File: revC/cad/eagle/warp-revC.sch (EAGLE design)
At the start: 13 parts, among them J2 QIIC connector, J3 QIIC connector, J4 DF40FC-20DP-0.4V(51), J5 CORTEX_DEBUG_SMD, U1 MAX40200, U2 MAX40200

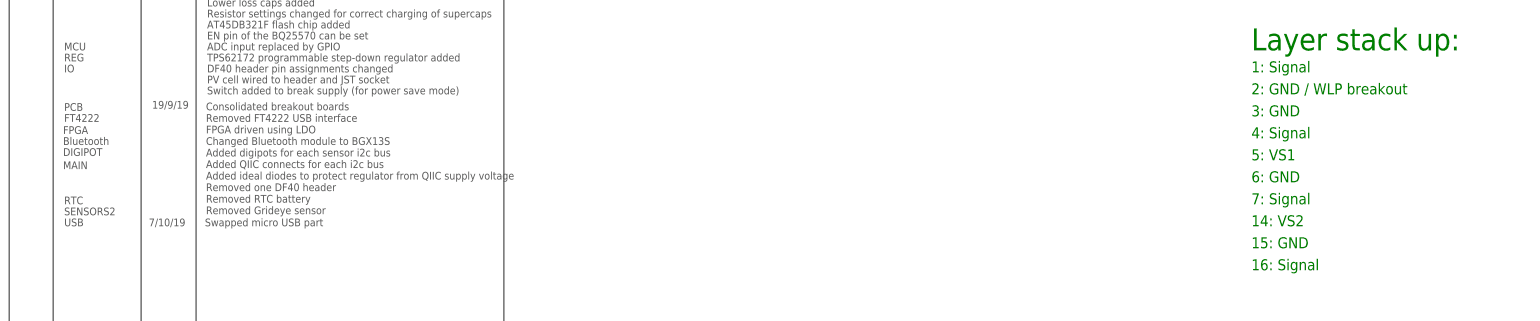
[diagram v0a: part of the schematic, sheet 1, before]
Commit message: Removed FPGA microvias and rerouted
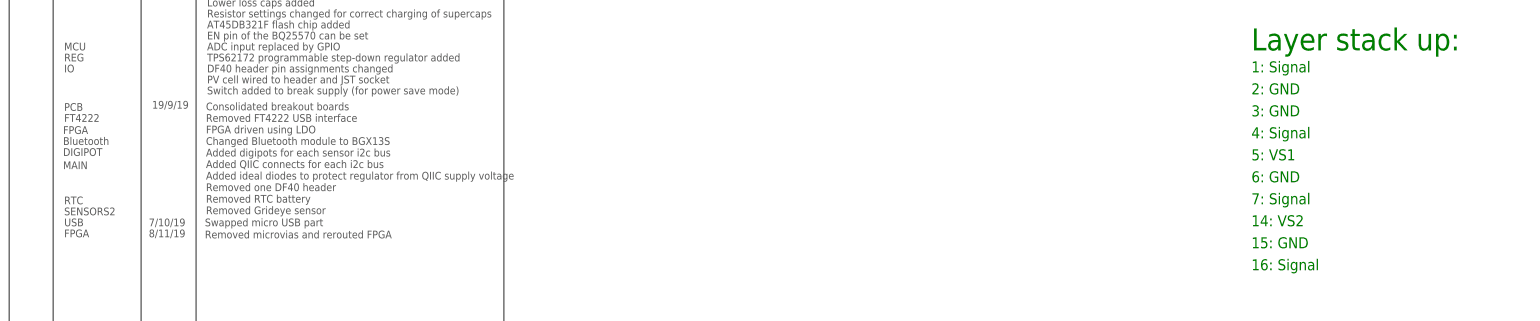
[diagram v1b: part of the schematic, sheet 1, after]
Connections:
- net GND: now also U2.IOB_25B_G3, U2.RGB1
- net VCC: now also U2.IOB_12A_G4_CDONE, U2.IOB_2A; no longer U2.VCCIO_0
- net VCC_1V2: now also U2.IOB_10A, U2.IOT_46B_G0, U2.VCCIO_0
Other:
- note added: "2: GND"
- note added: "8/11/19"
- note added: "Removed microvias and rerouted FPGA"
- note removed: "2: GND / WLP breakout"
- note removed: "USB2"
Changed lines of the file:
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@@
 <part name="C7" library="SparkFun-Passives" deviceset="CAP" device="0402-CAP" value="0.1uF"/>
 <part name="C6" library="SparkFun-Passives" deviceset="CAP" device="0402-CAP" value="10uF"/>
+<part name="GND4" library="supply1" library_urn="urn:adsk.eagle:library:371" deviceset="GND" device=""/>
+<part name="SUPPLY1" library="SparkFun-PowerSymbols" deviceset="VCC" device=""/>
+<part name="SUPPLY2" library="SparkFun-PowerSymbols" deviceset="VCC" device=""/>
+<part name="GND5" library="supply1" library_urn="urn:adsk.eagle:library:371" deviceset="GND" device=""/>
 </parts>
 <sheets>
@@
 <attribute name="NAME" x="313.944" y="114.681" size="1.778" layer="95"/>
 <attribute name="VALUE" x="313.944" y="109.601" size="1.778" layer="96"/>
+</instance>
+<instance part="GND4" gate="1" x="195.58" y="116.84" smashed="yes">
+<attribute name="VALUE" x="193.04" y="114.3" size="1.778" layer="96"/>
+</instance>
+<instance part="SUPPLY1" gate="G$1" x="198.12" y="144.78" smashed="yes">
+<attribute name="VALUE" x="198.12" y="147.574" size="1.778" layer="96" align="bottom-center"/>
+</instance>
+<instance part="SUPPLY2" gate="G$1" x="182.88" y="66.04" smashed="yes">
+<attribute name="VALUE" x="182.88" y="68.834" size="1.778" layer="96" align="bottom-center"/>
+</instance>
+<instance part="GND5" gate="1" x="193.04" y="66.04" smashed="yes">
+<attribute name="VALUE" x="190.5" y="63.5" size="1.778" layer="96"/>
 </instance>
 </instances>
@@
 <pinref part="C3" gate="G$1" pin="1"/>
 </segment>
+<segment>
+<pinref part="U2" gate="G$1" pin="IOB_10A"/>
+<wire x1="175.26" y1="144.78" x2="190.5" y2="144.78" width="0.1524" layer="91"/>
+<label x="177.8" y="144.78" size="1.778" layer="95"/>
+</segment>
+<segment>
+<pinref part="U2" gate="G$1" pin="IOT_46B_G0"/>
+<wire x1="175.26" y1="76.2" x2="187.96" y2="76.2" width="0.1524" layer="91"/>
+<label x="177.8" y="76.2" size="1.778" layer="95"/>
+</segment>
+<segment>
+<pinref part="U2" gate="G$1" pin="VCCIO_0"/>
+<wire x1="175.26" y1="165.1" x2="190.5" y2="165.1" width="0.1524" layer="91"/>
+<label x="177.8" y="165.1" size="1.778" layer="95"/>
+</segment>
 </net>
 <net name="I2C1_SCL" class="0">
@@
 <pinref part="C4" gate="G$1" pin="1"/>
 <pinref part="C5" gate="G$1" pin="1"/>
+<label x="177.8" y="134.62" size="1.778" layer="95"/>
 </segment>
 </net>
@@
 <pinref part="C2" gate="G$1" pin="2"/>
 </segment>
+<segment>
+<pinref part="U2" gate="G$1" pin="IOB_25B_G3"/>
+<wire x1="175.26" y1="114.3" x2="187.96" y2="114.3" width="0.1524" layer="91"/>
+<wire x1="187.96" y1="114.3" x2="187.96" y2="121.92" width="0.1524" layer="91"/>
+<wire x1="187.96" y1="121.92" x2="195.58" y2="121.92" width="0.1524" layer="91"/>
+<wire x1="195.58" y1="121.92" x2="195.58" y2="119.38" width="0.1524" layer="91"/>
+<pinref part="GND4" gate="1" pin="GND"/>
+<label x="177.8" y="114.3" size="1.778" layer="95"/>
+</segment>
+<segment>
+<pinref part="U2" gate="G$1" pin="RGB1"/>
+<wire x1="175.26" y1="71.12" x2="180.34" y2="71.12" width="0.1524" layer="91"/>
+<wire x1="180.34" y1="71.12" x2="180.34" y2="73.66" width="0.1524" layer="91"/>
+<wire x1="180.34" y1="73.66" x2="193.04" y2="73.66" width="0.1524" layer="91"/>
+<wire x1="193.04" y1="73.66" x2="193.04" y2="68.58" width="0.1524" layer="91"/>
+<pinref part="GND5" gate="1" pin="GND"/>
+</segment>
 </net>
 <net name="CRESET_B" class="0">
@@
 <net name="VCC" class="0">
 <segment>
-<label x="177.8" y="165.1" size="1.778" layer="95"/>
-<pinref part="U2" gate="G$1" pin="VCCIO_0"/>
-<wire x1="175.26" y1="165.1" x2="198.12" y2="165.1" width="0.1524" layer="91"/>
-<wire x1="198.12" y1="165.1" x2="198.12" y2="167.64" width="0.1524" layer="91"/>
 <label x="177.8" y="160.02" size="1.778" layer="95"/>
 <pinref part="U2" gate="G$1" pin="VCCIO_2"/>
 <wire x1="198.12" y1="167.64" x2="198.12" y2="175.26" width="0.1524" layer="91"/>
 <wire x1="175.26" y1="160.02" x2="198.12" y2="160.02" width="0.1524" layer="91"/>
-<wire x1="198.12" y1="160.02" x2="198.12" y2="165.1" width="0.1524" layer="91"/>
-<junction x="198.12" y="165.1"/>
+<wire x1="198.12" y1="160.02" x2="198.12" y2="167.64" width="0.1524" layer="91"/>
 <pinref part="VCC" gate="VCC" pin="VCC"/>
 <wire x1="175.26" y1="167.64" x2="198.12" y2="167.64" width="0.1524" layer="91"/>
@@
 <wire x1="53.34" y1="157.48" x2="53.34" y2="149.86" width="0.1524" layer="91"/>
 <pinref part="P+2" gate="VCC" pin="VCC"/>
+</segment>
+<segment>
+<pinref part="U2" gate="G$1" pin="IOB_12A_G4_CDONE"/>
+<wire x1="175.26" y1="139.7" x2="198.12" y2="139.7" width="0.1524" layer="91"/>
+<wire x1="198.12" y1="139.7" x2="198.12" y2="144.78" width="0.1524" layer="91"/>
+<pinref part="SUPPLY1" gate="G$1" pin="VCC"/>
+<label x="177.8" y="139.7" size="1.778" layer="95"/>
+</segment>
+<segment>
+<pinref part="U2" gate="G$1" pin="IOB_2A"/>
+<wire x1="175.26" y1="60.96" x2="182.88" y2="60.96" width="0.1524" layer="91"/>
+<wire x1="182.88" y1="60.96" x2="182.88" y2="66.04" width="0.1524" layer="91"/>
+<pinref part="SUPPLY2" gate="G$1" pin="VCC"/>
 </segment>
 </net>
@@
 Richard Hopper</text>
 <text x="293.624" y="6.096" size="1.778" layer="94">NO WARRANTY. See LICENCE.txt</text>
-<text x="344.17" y="20.32" size="2.54" layer="94" ratio="15">USB2</text>
+<text x="344.17" y="20.32" size="2.54" layer="94" ratio="15">USB</text>
 </plain>
 <instances>
@@
 <text x="304.8" y="101.6" size="5.08" layer="91">Layer stack up:</text>
 <text x="304.8" y="96.52" size="2.54" layer="91">1: Signal</text>
-<text x="304.8" y="91.44" size="2.54" layer="91">2: GND / WLP breakout</text>
+<text x="304.8" y="91.44" size="2.54" layer="91">2: GND</text>
 <text x="304.8" y="86.36" size="2.54" layer="91">3: GND</text>
 <text x="304.8" y="60.96" size="2.54" layer="91">14: VS2</text>
@@
 <text x="50.038" y="60.96" size="1.778" layer="97">7/10/19</text>
 <text x="62.992" y="60.96" size="1.778" layer="97">Swapped micro USB part </text>
+<text x="30.48" y="58.42" size="1.778" layer="97">FPGA</text>
+<text x="50.038" y="58.42" size="1.778" layer="97">8/11/19</text>
+<text x="62.992" y="58.166" size="1.778" layer="97">Removed microvias and rerouted FPGA</text>
 </plain>
 <instances>

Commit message: MAG3110 with FXOS8700CQ. Added BOM
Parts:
- removed U1, U2: MAX40200, MAX40200:MAX40200
- added S3: EVPAYG0BAEVPAYG0BA, EVPAYG0BA:EVPAYG0BAEVPAYG0BA
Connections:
- removed net !INT: U1.!INT!
- removed net !RESET: U1.!RESET
- removed net ADXL362_SPI_CS: U1.!CS
- removed net AT45DB321F_SPI_CS: U1.PTA9, U2.!CS!
- removed net BQ24230_OUT: U1.EN2, U1.OUT, U2.IN
- removed net CAP: U2.CAP
- removed net CRESET_B: U2.CRESET_B
- removed net CTRL: U1.CTRL
- removed net DCP_RW1: U1.RW
- removed net DCP_RW3: U2.RW
- removed net EXTAL0: U1.PTA3/EXTAL0
- removed net I2C_SCL: U1.SCL, U2.I2C_SCL/SPI_SPC, U2.SCX
- removed net I2C_SCL/LPUART0_TX: U1.PTB3/IRQ_10
- removed net I2C_SDA: U1.SDA, U2.I2C_SDA/SPI_SDI/SPI3_SDO, U2.SDX
- removed net I2C_SDA/LPUART0_RX: U1.PTB4/IRQ_11
- removed net ICE40_VCC_PLL: U2.IOB_24A, U2.VCCPLL
- removed net IN: U1.IN
- removed net LBOOST: U1.LBOOST
- removed net LBUCK: U1.LBUCK
- removed net LOAD: U1.LOAD
- removed net N$1: U1.BYP, U1.ISET, U1.LFXTAL_N
- removed net N$2: U1.ILIM, U1.LFXTAL_P
- removed net N$3: U1.!PGOOD!, U1.ANTENNA, U1.EVI, U1.RF
- removed net N$4: U1.TS, U2.!WP!
- removed net N$5: U1.!CHG!
- removed net N$8: U1.TMR
- removed net OK_HYST: U1.OK_HYST
- removed net OK_PROG: U1.OK_PROG
- removed net OUT: U2.OUT
- removed net PTA0/SWD_CLK: U1.PTA0/IRQ_0/LLWU_P7
- removed net PTA1/RESET_B: S1.A, S1.A', U1.PTA1/IRQ1/LPTMR0_ALT1
- removed net PTA12: U1.PTA12/IRQ_13/LPTMR0_ALT2
- removed net PTA2/SWD_DIO: U1.PTA2
- removed net PTA5: U1.PTA5/RTC_CLK_IN
- removed net PTA8: U1.PTA8
- removed net PTB1: U1.PTB1/IRQ_6/ADC0_SE8/CMP0_IN3
- removed net PTB10: U1.PTB10
- removed net PTB11: U1.PTB11
- removed net PTB13/CLKOUT32K: U1.PTB13/CLKOUT32K
- removed net PTB2: U1.PTB2/IRQ_7
- removed net PTB5: U1.PTB5/IRQ_12
- removed net PTB6: U1.PTB6/IRQ_2/LPTMR0_ALT3
- removed net PTB7: U1.PTB7/IRQ_3
- removed net REG_LOAD: U1.IN
- removed net SPI_CS: U1.CS, U2.CS, U2.IOB_35B_SPI_SS
- removed net SPI_MISO: U1.MISO, U1.PTA6, U1.SDO, U2.IOB_32A_SPI_SO, U2.SDO, U2.SO
- removed net SPI_MOSI: U1.MOSI, U1.PTA7/IRQ_4, U1.SDI, U2.IOB_33B_SPI_SI, U2.SDI, U2.SI
- removed net SW: U1.SW
- removed net UART_CTS: U1.UART_CTS
- removed net UART_RTS: U1.UART_RTS
- removed net UART_RX: U1.UART_RX
- removed net UART_TX: U1.UART_TX
- removed net VBAT: U1.VBAT
- removed net VBAT_OV: U1.VBAT_OV
- removed net VBUS: U1.VBUS
- removed net VCC: U1.IOVDD, U1.RL, U1.VBATT, U1.VCC, U1.VDD, U1.VDDIO, U1.VLOGIC, U1.VS, U2.!RST!, U2.I2C_VS_SPI_MODE_SELECT, U2.IOB_12A_G4_CDONE, U2.IOB_2A, U2.PS, U2.RL, U2.SPI_VCCIO1, U2.VCC, U2.VCCIO_2, U2.VDD, U2.VDDIO, U2.VDD_IO, U2.VLOGIC, U2.VPP_2V5
- removed net VCC_1V2: U1.OUT, U2.IOB_10A, U2.IOT_46B_G0, U2.VCC, U2.VCCIO_0
- removed net VIN: U1.EN, U1.VIN, U1.VIN_DC
- removed net VOUT: U1.VOUT
- removed net VOUT_SET: U1.VOUT_SET
- removed net VRDIV: U1.VRDIV
- removed net VREF_SAMP: U1.VREF_SAMP
- removed net VREG: U1.IN
- removed net VSEL1: U1.VSEL1
- removed net VSEL2: U1.VSEL2
- removed net VSEL3: U1.VSEL3
- removed net VSEL4: U1.VSEL4
- removed net VSTOR: U1.VOC_SAMP, U1.VOUT_EN, U1.VSTOR
- removed net XTAL0: U1.PTA4/XTAL0
- net BAT: no longer U1.BAT
- net GND: now also S3.B, S3.B'; no longer S1.B, S1.B', U1.!CE!, U1.!EN, U1.ANT_GND, U1.CLKOE, U1.EN1, U1.GND, U1.GND@10, U1.GND@12, U1.GND@13, U1.GND@16, U1.GND@5, U1.NC17, U1.NC9, U1.PAD, U1.SA0, U1.SHIELD, U1.TD, U1.VGND, U1.VSS, U1.VSS1, U1.VSS15, U2.CSB3, U2.GND, U2.GND@12, U2.GND@13, U2.GNDA, U2.GNDIO, U2.I2C_SA0/SPI_SDO, U2.IOB_25B_G3, U2.RESERVED@10, U2.RESERVED@11, U2.RESERVED@15, U2.RESERVED@9, U2.RGB1, U2.SDO1, U2.SDO2, U2.VGND
- net I2C1_SCL: no longer U2.IOT_47A
- net I2C1_SDA: no longer U2.IOB_11B_G5
- net I2C2_SCL: no longer U2.IOT_37A
- net I2C2_SDA: no longer U2.IOT_36B
- net RTC_!INT!/RESET_B: now also S3.A, S3.A'
- net SPI_SCK: no longer U1.PTB0/IRQ_5/LLWU_P4, U1.SCK, U1.SCLK, U2.IOB_34A_SPI_SCK, U2.SCK
- net VCC_QIIC: no longer U2.IN
- net VS2: no longer U1.OUT, U2.OUT
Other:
- note added: "13/11/19"
- note added: "14/11/19"
- note added: "BLUETHOOTH"
- note added: "BOARD"
- note added: "Brought reset switch out to main sheet"
- note added: "External sensor sockets"
- note added: "Header breakout socket"
- note added: "I2C Address: 0x1E"
- note added: "Ideal dioides placed in module"
- note added: "MCU reset switch"
- note added: "MODULE ABBEVIATIONS BT: BLUETHOOTH CH: CHARGER DP: DIGIPOT FP: FPGA MP: MPU PV: BOOSTER RG: REG RT: RTC SA: SENSORS-A SB: SENSORS-B USB: USB"
- note added: "Replaced MAG3110 (obsolete) with FXOS8700CQ"
- note added: "SENSOR"
- note added: "SENSORS"
- note added: "Supply switching for FPGA"
- note removed: "Bluetooth"
- note removed: "External sensor socket"
- note removed: "Header sockets"
- note removed: "I2C Address: 0x0E"
- note removed: "PCB"
- note removed: "Reset switch"
- note removed: "SENSORS2"
- note removed: "Supply select for FPGA"
- moved on the sheet: J5

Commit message: Corrected footprint errors
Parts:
- J5: value CORTEX_DEBUG_SMD -> CORTEX_DEBUGCORTEX_DEBUG; device SparkFun-Connectors:CORTEX_DEBUG_SMD -> CORTEX_DEBUG:CORTEX_DEBUGCORTEX_DEBUG
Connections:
- net BGX13S_!RST renamed FPGA_CS
- net SI4705_!RST renamed CRESET_B
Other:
- moved on the sheet: J5

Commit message: Corrections to footprints
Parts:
- removed FD1, FD2, FD3, FD4: FIDUCIAL1X2, SparkFun-Aesthetics:FIDUCIAL1X2
- J5: value CORTEX_DEBUGCORTEX_DEBUG -> FTSH-105-01-XXX-DV-K; device CORTEX_DEBUG:CORTEX_DEBUGCORTEX_DEBUG -> FTSH-105-01-XXX-DV-K:FTSH-105-01-XXX-DV-K
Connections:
- net GND: now also J5.3, J5.5; no longer J5.GND@3, J5.GND@5
- net RTC_!INT!/RESET_B: now also J5.10; no longer J5.!RESET
- net SWD_CLK: now also J5.4; no longer J5.SWDCLK/TCK
- net SWD_DIO: now also J5.2; no longer J5.SWDIO/TMS
- net VS1: now also J5.1; no longer J5.VCC
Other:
- note removed: "Fiducial Markers"
- moved on the sheet: J5

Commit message: Commit of CAD design, BOM and datasheets for 1st production run of Warp-revC
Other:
- note added: "15/01/19"
- note added: "Corrected SPI lines from MCU"
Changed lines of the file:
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@@
 <text x="62.738" y="50.546" size="1.778" layer="97">Replaced MAG3110 (obsolete) with FXOS8700CQ</text>
 <text x="50.038" y="50.8" size="1.778" layer="97">14/11/19</text>
+<text x="50.038" y="48.26" size="1.778" layer="97">15/01/19</text>
+<text x="62.738" y="48.006" size="1.778" layer="97">Corrected SPI lines from MCU</text>
+<text x="30.48" y="48.26" size="1.778" layer="97">MCU</text>
 </plain>
 <instances>
@@
 </segment>
 <segment>
-<portref moduleinst="MP" port="SPI_MISO"/>
-<wire x1="144.78" y1="185.42" x2="195.58" y2="185.42" width="0.1524" layer="91"/>
-<label x="165.1" y="185.42" size="1.778" layer="95"/>
-</segment>
-<segment>
 <portref moduleinst="FP" port="SPI_MOSI"/>
 <wire x1="144.78" y1="27.94" x2="109.22" y2="27.94" width="0.1524" layer="91"/>
@@
 <label x="325.12" y="86.36" size="1.778" layer="95"/>
 </segment>
+<segment>
+<wire x1="144.78" y1="187.96" x2="195.58" y2="187.96" width="0.1524" layer="91"/>
+<label x="167.64" y="187.96" size="1.778" layer="95"/>
+<portref moduleinst="MP" port="SPI_MOSI"/>
+</segment>
 </net>
 <net name="SPI_MISO/UART_RTS" class="0">
-<segment>
-<portref moduleinst="MP" port="SPI_MOSI"/>
-<wire x1="144.78" y1="187.96" x2="195.58" y2="187.96" width="0.1524" layer="91"/>
-<label x="165.1" y="187.96" size="1.778" layer="95"/>
-</segment>
 <segment>
 <portref moduleinst="SA" port="SPI_MISO"/>
@@
 <label x="325.12" y="88.9" size="1.778" layer="95"/>
 </segment>
-</net>
+<segment>
+<wire x1="144.78" y1="185.42" x2="195.58" y2="185.42" width="0.1524" layer="91"/>
+<label x="167.64" y="185.42" size="1.778" layer="95"/>
+<portref moduleinst="MP" port="SPI_MISO"/>
+</segment>
+</net>
